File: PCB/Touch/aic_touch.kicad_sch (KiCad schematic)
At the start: 18 parts, among them J1 Antenna, J2 PN5180, J3 PN532, J4 Display, J5 Antenna, U1 Pico

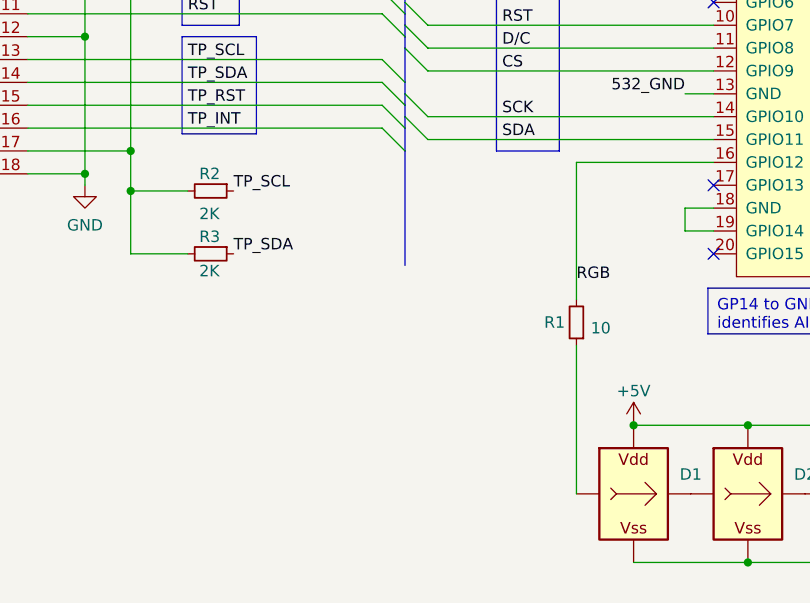
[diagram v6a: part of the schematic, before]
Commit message: Touch PCB v1.51, optimize footprints
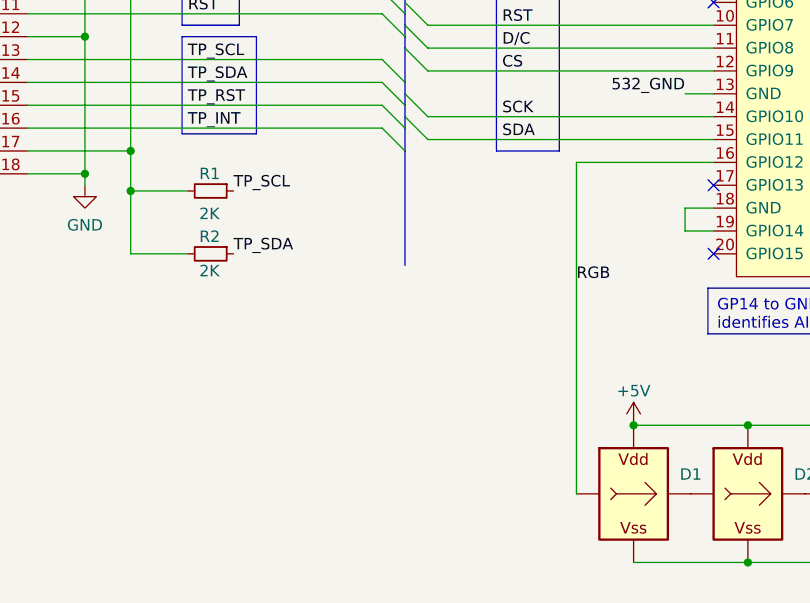
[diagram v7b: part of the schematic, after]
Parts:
- removed R1: 10, Resistor_SMD:R_0603_1608Metric, symbol Device:R_Small
- C1, C2, C3: footprint Capacitor_SMD:C_0603_1608Metric -> Capacitor_SMD:C_0603_1608Metric_Pad1.08x0.95mm_HandSolder
- R1: renamed from R2; footprint Resistor_SMD:R_0603_1608Metric -> Resistor_SMD:R_0603_1608Metric_Pad0.98x0.95mm_HandSolder
- R2: renamed from R3; footprint Resistor_SMD:R_0603_1608Metric -> Resistor_SMD:R_0603_1608Metric_Pad0.98x0.95mm_HandSolder
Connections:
- net RGB: now also D1.I (In)
